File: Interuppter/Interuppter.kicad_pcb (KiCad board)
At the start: 2 copper layers, 116.1 x 55.5 mm, 93 parts, among them J1 Conn_01x03, J2 Conn_01x03, J4 USB_C_Receptacle_USB2.0_16P, J5 Display, SW1 BUTTON, SW2 BUT_START, SW3 BUTTON, SW4 SW_SPST, U1 RP2350A, U2 DRL2180_OUT, U3 W25Q32JVSS, U4 TLV62130RGT, U5 DRL2180_IN, U6 IP2326, U7 USBLC6-2SC6, Y1 12MHz

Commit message: Update KiCAD and add GERBER files and 3D screenshots
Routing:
- net +3.3V: track 41.7 -> 38.8 mm, vias 10 -> 12
- net +1V1: track 28.7 -> 29.9 mm
- net GND: track 81.8 -> 80.6 mm, vias 93 -> 92
- net +BATT: track 147.9 -> 148.3 mm, vias 7 -> 9
- net /Power_3.3V/BUT: track 93.0 -> 93.2 mm, vias 2 -> 4
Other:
- board text added: "KiCAD development"
- board text added: "Uki_chan228"

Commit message: Update KiCAD and add GERBER files and 3D screenshots
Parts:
- J1: footprint Conn_JST:JST_ZH_S3B-ZR-SM4A-TF_1x03-1MP_P1.50mm_Horizontal -> Connector_Molex:Molex_PicoBlade_53261-0371_1x03-1MP_P1.25mm_Horizontal
- J2: footprint Conn_JST:JST_GH_SM03B-GHS-TB_1x03-1MP_P1.25mm_Horizontal -> Connector_Molex:Molex_PicoBlade_53261-0371_1x03-1MP_P1.25mm_Horizontal
- moved J1 1.18 mm to (218.2, 101.5)
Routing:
- net /Power_3.3V/BUT: track 93.2 -> 95.8 mm

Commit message: Update C++ code
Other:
- board text added: "1"
- board text added: "14"
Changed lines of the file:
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@@
+		)
+	)
+	(gr_text "14\n"
+		(at 174.7225 126.8 0)
+		(layer "F.SilkS")
+		(effects
+			(font
+				(size 1.5 1.5)
+				(thickness 0.3)
+				(bold yes)
+			)
+			(justify left bottom)
+		)
+	)
+	(gr_text "1"
+		(at 175.0625 142.09 0)
+		(layer "F.SilkS")
+		(effects
+			(font
+				(size 1.5 1.5)
+				(thickness 0.3)
+				(bold yes)
+			)
+			(justify left bottom)
 		)
 	)

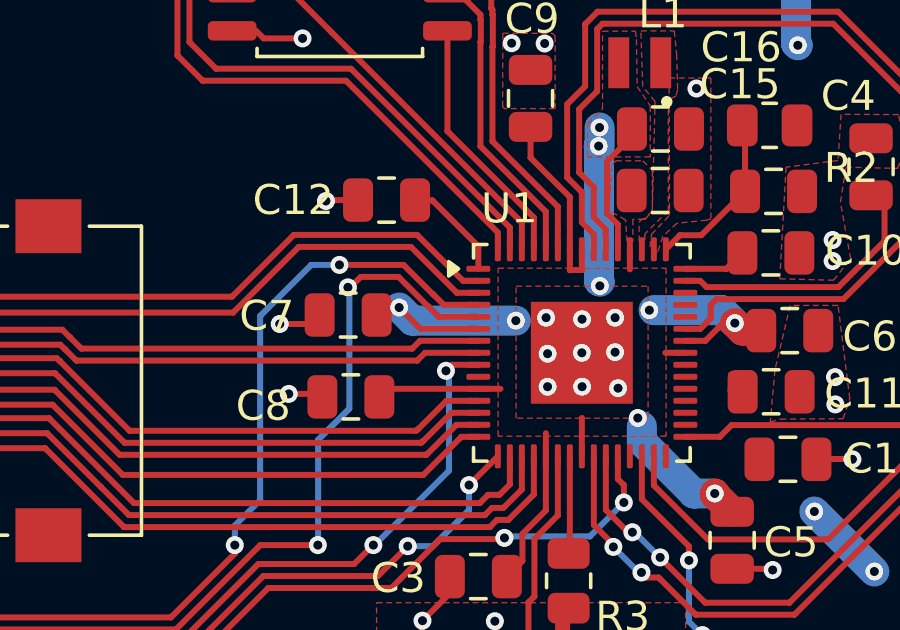
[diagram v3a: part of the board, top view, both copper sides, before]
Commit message: Update C++ code. Added headers and drivers for I2C pio and SPI PIO
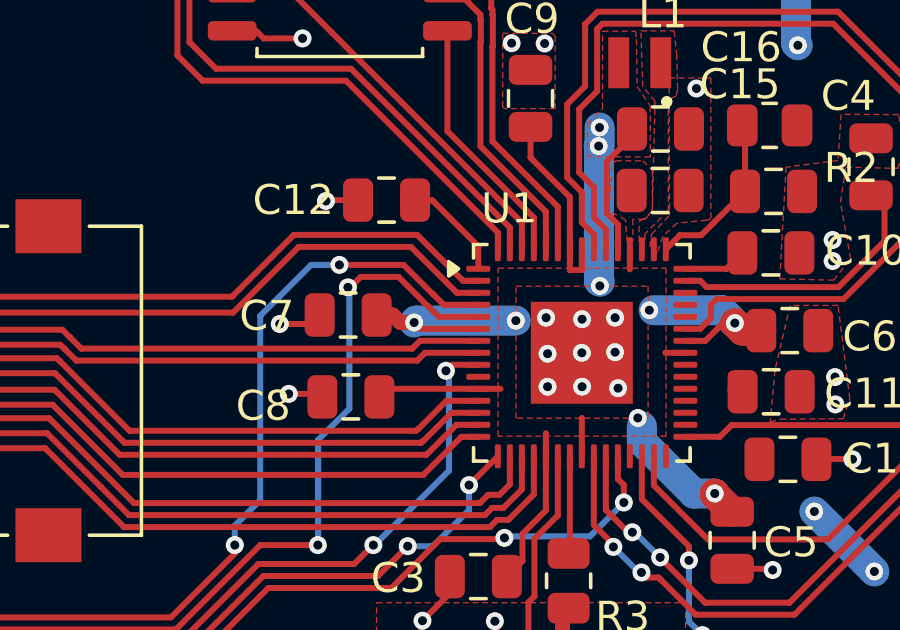
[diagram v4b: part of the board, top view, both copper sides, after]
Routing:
- net +1V1: track 29.9 -> 29.1 mm
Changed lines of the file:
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@@
 	)
 	(segment
-		(start 191.0025 131.1)
-		(end 190.5025 131.1)
-		(width 0.5)
+		(start 201.994546 131.422046)
+		(end 201.9925 131.422046)
+		(width 0.2)
+		(layer "F.Cu")
+		(net "+1V1")
+	)
+	(segment
+		(start 191.5025 131.6)
+		(end 191.0425 131.6)
+		(width 0.5)
+		(layer "F.Cu")
+		(net "+1V1")
+	)
+	(segment
+		(start 190.2525 131.12)
+		(end 190.2625 131.11)
+		(width 0.5)
+		(layer "F.Cu")
+		(net "+1V1")
+	)
+	(segment
+		(start 201.5225 137.33)
+		(end 202.1025 137.91)
+		(width 1)
+		(layer "F.Cu")
+		(net "+1V1")
+	)
+	(segment
+		(start 197.9325 127.968629)
+		(end 197.9325 126.23)
+		(width 0.2)
+		(layer "F.Cu")
+		(net "+1V1")
+	)
+	(segment
+		(start 201.656365 131.758181)
+		(end 201.656365 131.761821)
+		(width 0.2)
+		(layer "F.Cu")
+		(net "+1V1")
+	)
+	(segment
+		(start 202.1925 131.62)
+		(end 201.8925 131.62)
+		(width 0.2)
+		(layer "F.Cu")
+		(net "+1V1")
+	)
+	(segment
+		(start 201.5225 137.3)
+		(end 201.5225 137.33)
+		(width 1)
+		(layer "F.Cu")
+		(net "+1V1")
+	)
+	(segment
+		(start 191.0425 131.6)
+		(end 190.7925 131.35)
+		(width 0.5)
+		(layer "F.Cu")
+		(net "+1V1")
+	)
+	(segment
+		(start 197.0925 136.06)
+		(end 197.0925 134.78)
+		(width 0.2)
+		(layer "F.Cu")
+		(net "+1V1")
+	)
+	(segment
+		(start 202.1925 131.62)
+		(end 201.994546 131.422046)
+		(width 0.2)
+		(layer "F.Cu")
+		(net "+1V1")
+	)
+	(segment
+		(start 190.7925 131.35)
+		(end 190.2525 131.35)
+		(width 0.5)
+		(layer "F.Cu")
+		(net "+1V1")
+	)
+	(segment
+		(start 202.4425 131.87)
+		(end 202.1925 131.62)
+		(width 1)
+		(layer "F.Cu")
+		(net "+1V1")
+	)
+	(segment
+		(start 201.8925 131.62)
+		(end 201.8425 131.57)
+		(width 0.2)
+		(layer "F.Cu")
+		(net "+1V1")
+	)
+	(segment
+		(start 198.7625 125.4)
+		(end 198.7625 125.15)
+		(width 0.2)
+		(layer "F.Cu")
+		(net "+1V1")
+	)
+	(segment
+		(start 198.2925 128.32863)
+		(end 197.9325 127.968629)
+		(width 0.2)
+		(layer "F.Cu")
+		(net "+1V1")
+	)
+	(segment
+		(start 191.5025 131.6)
+		(end 191.7125 131.81)
+		(width 0.2)
+		(layer "F.Cu")
+		(net "+1V1")
+	)
+	(segment
+		(start 190.2525 131.35)
+		(end 190.2525 131.12)
+		(width 0.5)
+		(layer "F.Cu")
+		(net "+1V1")
+	)
+	(segment
+		(start 197.9325 126.23)
+		(end 198.7625 125.4)
+		(width 0.2)
+		(layer "F.Cu")
+		(net "+1V1")
+	)
+	(segment
+		(start 203.0725 131.87)
+		(end 202.4425 131.87)
+		(width 1)
 		(layer "F.Cu")
 		(net "+1V1")
@@
 	)
 	(segment
-		(start 201.994546 131.422046)
-		(end 201.9925 131.422046)
-		(width 0.2)
-		(layer "F.Cu")
-		(net "+1V1")
-	)
-	(segment
-		(start 190.2525 131.12)
-		(end 190.2625 131.11)
-		(width 0.5)
-		(layer "F.Cu")
-		(net "+1V1")
-	)
-	(segment
-		(start 201.5225 137.33)
-		(end 202.1025 137.91)
-		(width 1)
-		(layer "F.Cu")
-		(net "+1V1")
-	)
-	(segment
-		(start 197.9325 127.968629)
-		(end 197.9325 126.23)
-		(width 0.2)
-		(layer "F.Cu")
-		(net "+1V1")
-	)
-	(segment
-		(start 201.656365 131.758181)
-		(end 201.656365 131.761821)
-		(width 0.2)
-		(layer "F.Cu")
-		(net "+1V1")
-	)
-	(segment
-		(start 202.1925 131.62)
-		(end 201.8925 131.62)
-		(width 0.2)
-		(layer "F.Cu")
-		(net "+1V1")
-	)
-	(segment
-		(start 201.5225 137.3)
-		(end 201.5225 137.33)
-		(width 1)
-		(layer "F.Cu")
-		(net "+1V1")
-	)
-	(segment
-		(start 197.0925 136.06)
-		(end 197.0925 134.78)
-		(width 0.2)
-		(layer "F.Cu")
-		(net "+1V1")
-	)
-	(segment
-		(start 202.1925 131.62)
-		(end 201.994546 131.422046)
-		(width 0.2)
-		(layer "F.Cu")
-		(net "+1V1")
-	)
-	(segment
-		(start 202.4425 131.87)
-		(end 202.1925 131.62)
-		(width 1)
-		(layer "F.Cu")
-		(net "+1V1")
-	)
-	(segment
-		(start 201.8925 131.62)
-		(end 201.8425 131.57)
-		(width 0.2)
-		(layer "F.Cu")
-		(net "+1V1")
-	)
-	(segment
-		(start 198.7625 125.4)
-		(end 198.7625 125.15)
-		(width 0.2)
-		(layer "F.Cu")
-		(net "+1V1")
-	)
-	(segment
-		(start 198.2925 128.32863)
-		(end 197.9325 127.968629)
-		(width 0.2)
-		(layer "F.Cu")
-		(net "+1V1")
-	)
-	(segment
-		(start 190.2525 131.35)
-		(end 190.2525 131.12)
-		(width 0.5)
-		(layer "F.Cu")
-		(net "+1V1")
-	)
-	(segment
-		(start 197.9325 126.23)
-		(end 198.7625 125.4)
-		(width 0.2)
-		(layer "F.Cu")
-		(net "+1V1")
-	)
-	(segment
-		(start 191.0025 131.1)
-		(end 191.7125 131.81)
-		(width 0.2)
-		(layer "F.Cu")
-		(net "+1V1")
-	)
-	(segment
-		(start 203.0725 131.87)
-		(end 202.4425 131.87)
-		(width 1)
-		(layer "F.Cu")
-		(net "+1V1")
-	)
-	(segment
 		(start 201.208185 132.21)
 		(end 200.5425 132.21)
@@
 	)
 	(segment
-		(start 190.5025 131.1)
-		(end 190.2525 131.35)
-		(width 0.5)
-		(layer "F.Cu")
-		(net "+1V1")
-	)
-	(segment
 		(start 201.656365 131.761821)
 		(end 201.208185 132.21)
@@
 	)
 	(via
-		(at 191.0025 131.1)
+		(at 191.5025 131.6)
 		(size 0.6)
 		(drill 0.3)
@@
 	)
 	(segment
+		(start 191.564563 131.537937)
+		(end 194.892498 131.537937)
+		(width 1)
+		(layer "B.Cu")
+		(net "+1V1")
+	)
+	(segment
 		(start 197.6825 125.75)
 		(end 197.6825 125.1)
@@
 	)
 	(segment
-		(start 191.440437 131.537937)
-		(end 191.0025 131.1)
-		(width 1)
-		(layer "B.Cu")
-		(net "+1V1")
-	)
-	(segment
 		(start 197.6925 130.24)
 		(end 197.6625 130.21)
@@
 	)
 	(segment
-		(start 194.892498 131.537937)
-		(end 191.440437 131.537937)
-		(width 1)
-		(layer "B.Cu")
+		(start 191.5025 131.6)
+		(end 191.564563 131.537937)
+		(width 1)
+		(layer "B.Cu")
